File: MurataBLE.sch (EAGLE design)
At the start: 46 parts, among them CON1 C-2235, IC1 I-5448, IC3 74LVC1G00DBV, Q1 FC-135 32.7680KA-AG3, Q2 12MHz, SW1 P8073, SW2 P8073, SW3 P8073, U1 IC_BLE_LBCA2HNZYZ-711, X1 TSW-114-02-S-S

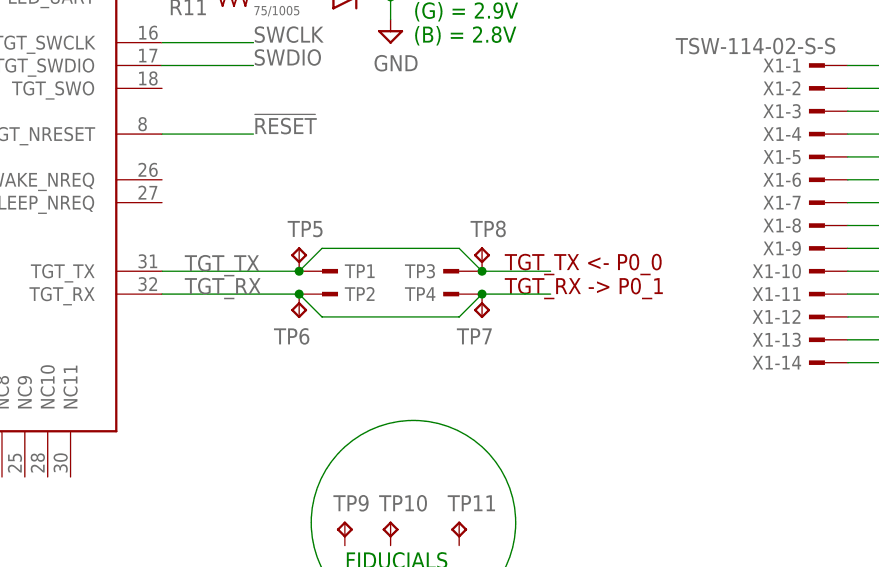
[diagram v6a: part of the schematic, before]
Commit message: [ USB ][ SCH ] test pads are connected
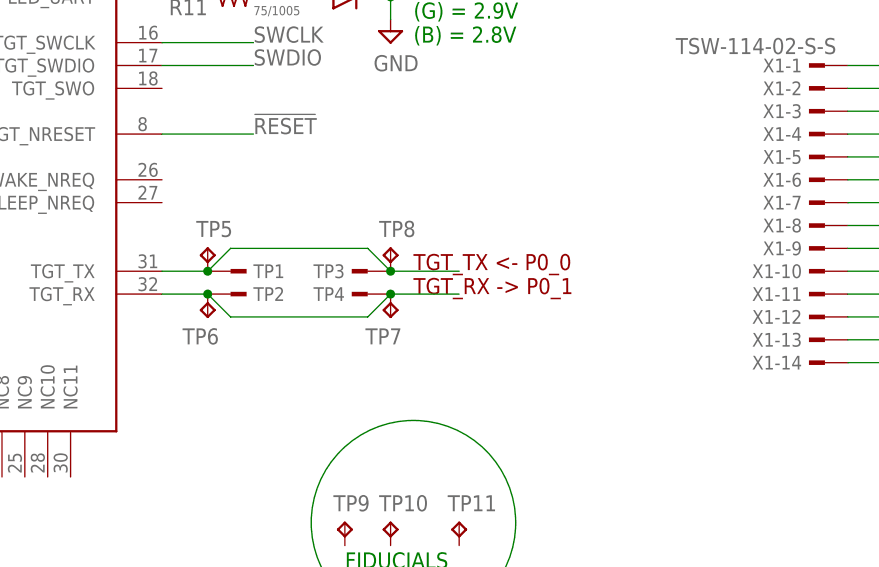
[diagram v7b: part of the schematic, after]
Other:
- moved on the sheet: TP1, TP2, TP3, TP4, TP5, TP6, TP7, TP8
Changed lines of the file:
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@@
 (G) = 2.9V
 (B) = 2.8V</text>
-<text x="195.58" y="68.58" size="1.778" layer="94">TGT_TX &lt;- P0_0
+<text x="185.42" y="68.58" size="1.778" layer="94">TGT_TX &lt;- P0_0
 TGT_RX -&gt; P0_1</text>
 <text x="233.68" y="139.7" size="1.778" layer="94">P0_0 -&gt; TGT_TX
@@
 <instance part="LED1" gate="G" x="175.26" y="104.14" rot="R90"/>
 <instance part="LED1" gate="B" x="177.8" y="101.6" rot="R90"/>
-<instance part="TP5" gate="G$1" x="172.72" y="73.66"/>
-<instance part="TP6" gate="G$1" x="172.72" y="66.04" rot="R180"/>
-<instance part="TP7" gate="G$1" x="193.04" y="66.04" rot="R180"/>
-<instance part="TP8" gate="G$1" x="193.04" y="73.66"/>
+<instance part="TP5" gate="G$1" x="162.56" y="73.66"/>
+<instance part="TP6" gate="G$1" x="162.56" y="66.04" rot="R180"/>
+<instance part="TP7" gate="G$1" x="182.88" y="66.04" rot="R180"/>
+<instance part="TP8" gate="G$1" x="182.88" y="73.66"/>
 <instance part="X1" gate="-1" x="231.14" y="93.98" rot="MR0"/>
 <instance part="X1" gate="-2" x="231.14" y="91.44" rot="MR0"/>
@@
 <instance part="X1" gate="-13" x="231.14" y="63.5" rot="MR0"/>
 <instance part="X1" gate="-14" x="231.14" y="60.96" rot="MR0"/>
-<instance part="TP1" gate="1" x="175.26" y="71.12"/>
-<instance part="TP2" gate="1" x="175.26" y="68.58"/>
-<instance part="TP3" gate="1" x="190.5" y="71.12" rot="R180"/>
-<instance part="TP4" gate="1" x="190.5" y="68.58" rot="R180"/>
+<instance part="TP1" gate="1" x="165.1" y="71.12"/>
+<instance part="TP2" gate="1" x="165.1" y="68.58"/>
+<instance part="TP3" gate="1" x="180.34" y="71.12" rot="R180"/>
+<instance part="TP4" gate="1" x="180.34" y="68.58" rot="R180"/>
 <instance part="TP9" gate="G$1" x="177.8" y="43.18"/>
 <instance part="TP10" gate="G$1" x="182.88" y="43.18"/>
@@
 <segment>
 <pinref part="IC2" gate="G$1" pin="TGT_TX"/>
-<label x="160.02" y="71.12" size="1.778" layer="95"/>
-<wire x1="172.72" y1="71.12" x2="157.48" y2="71.12" width="0.1524" layer="91"/>
+<wire x1="162.56" y1="71.12" x2="157.48" y2="71.12" width="0.1524" layer="91"/>
 <pinref part="TP5" gate="G$1" pin="TP"/>
-<junction x="172.72" y="71.12"/>
+<junction x="162.56" y="71.12"/>
 <pinref part="TP1" gate="1" pin="1"/>
-<wire x1="200.66" y1="71.12" x2="193.04" y2="71.12" width="0.1524" layer="91"/>
+<wire x1="190.5" y1="71.12" x2="182.88" y2="71.12" width="0.1524" layer="91"/>
 <pinref part="TP8" gate="G$1" pin="TP"/>
-<junction x="193.04" y="71.12"/>
+<junction x="182.88" y="71.12"/>
 <pinref part="TP3" gate="1" pin="1"/>
-<wire x1="172.72" y1="71.12" x2="175.26" y2="73.66" width="0.1524" layer="91"/>
-<wire x1="175.26" y1="73.66" x2="190.5" y2="73.66" width="0.1524" layer="91"/>
-<wire x1="190.5" y1="73.66" x2="193.04" y2="71.12" width="0.1524" layer="91"/>
+<wire x1="162.56" y1="71.12" x2="165.1" y2="73.66" width="0.1524" layer="91"/>
+<wire x1="165.1" y1="73.66" x2="180.34" y2="73.66" width="0.1524" layer="91"/>
+<wire x1="180.34" y1="73.66" x2="182.88" y2="71.12" width="0.1524" layer="91"/>
 </segment>
 </net>
@@
 <net name="TGT_RX" class="0">
 <segment>
-<wire x1="200.66" y1="68.58" x2="193.04" y2="68.58" width="0.1524" layer="91"/>
+<wire x1="190.5" y1="68.58" x2="182.88" y2="68.58" width="0.1524" layer="91"/>
 <pinref part="TP7" gate="G$1" pin="TP"/>
-<junction x="193.04" y="68.58"/>
+<junction x="182.88" y="68.58"/>
 <pinref part="TP4" gate="1" pin="1"/>
 <pinref part="IC2" gate="G$1" pin="TGT_RX"/>
-<label x="160.02" y="68.58" size="1.778" layer="95"/>
-<wire x1="172.72" y1="68.58" x2="157.48" y2="68.58" width="0.1524" layer="91"/>
+<wire x1="162.56" y1="68.58" x2="157.48" y2="68.58" width="0.1524" layer="91"/>
 <pinref part="TP6" gate="G$1" pin="TP"/>
-<junction x="172.72" y="68.58"/>
+<junction x="162.56" y="68.58"/>
 <pinref part="TP2" gate="1" pin="1"/>
-<wire x1="193.04" y1="68.58" x2="190.5" y2="66.04" width="0.1524" layer="91"/>
-<wire x1="190.5" y1="66.04" x2="175.26" y2="66.04" width="0.1524" layer="91"/>
-<wire x1="175.26" y1="66.04" x2="172.72" y2="68.58" width="0.1524" layer="91"/>
-</segment>
-</net>
+<wire x1="182.88" y1="68.58" x2="180.34" y2="66.04" width="0.1524" layer="91"/>
+<wire x1="180.34" y1="66.04" x2="165.1" y2="66.04" width="0.1524" layer="91"/>
+<wire x1="165.1" y1="66.04" x2="162.56" y2="68.58" width="0.1524" layer="91"/>
+</segment>
+</net>

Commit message: [ USB ] fix broken schematic link
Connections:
- removed net P0_0: U1.P0_0, X1-5.1
- removed net P0_1: U1.P0_1, X1-4.1
- net TGT_RX: now also U1.P0_1, X1-4.1
- net TGT_TX: now also U1.P0_0, X1-5.1
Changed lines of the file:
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@@
-</segment>
-</net>
-<net name="P0_0" class="0">
-<segment>
-<pinref part="U1" gate="G$1" pin="P0_0"/>
-<wire x1="241.3" y1="142.24" x2="228.6" y2="142.24" width="0.1524" layer="91"/>
-</segment>
-<segment>
-<wire x1="233.68" y1="83.82" x2="241.3" y2="83.82" width="0.1524" layer="91"/>
-<label x="241.3" y="83.82" size="1.778" layer="95"/>
-<pinref part="X1" gate="-5" pin="1"/>
-</segment>
-</net>
-<net name="P0_1" class="0">
-<segment>
-<pinref part="U1" gate="G$1" pin="P0_1"/>
-<wire x1="241.3" y1="139.7" x2="228.6" y2="139.7" width="0.1524" layer="91"/>
-</segment>
-<segment>
-<wire x1="233.68" y1="86.36" x2="241.3" y2="86.36" width="0.1524" layer="91"/>
-<label x="241.3" y="86.36" size="1.778" layer="95"/>
-<pinref part="X1" gate="-4" pin="1"/>
 </segment>
 </net>
@@
 <wire x1="180.34" y1="73.66" x2="182.88" y2="71.12" width="0.1524" layer="91"/>
 </segment>
+<segment>
+<pinref part="U1" gate="G$1" pin="P0_0"/>
+<wire x1="241.3" y1="142.24" x2="228.6" y2="142.24" width="0.1524" layer="91"/>
+</segment>
+<segment>
+<wire x1="233.68" y1="83.82" x2="241.3" y2="83.82" width="0.1524" layer="91"/>
+<label x="241.3" y="83.82" size="1.778" layer="95"/>
+<pinref part="X1" gate="-5" pin="1"/>
+</segment>
 </net>
 <net name="N$4" class="0">
@@
 <wire x1="165.1" y1="66.04" x2="162.56" y2="68.58" width="0.1524" layer="91"/>
 </segment>
-</net>
+<segment>
+<pinref part="U1" gate="G$1" pin="P0_1"/>
+<wire x1="241.3" y1="139.7" x2="228.6" y2="139.7" width="0.1524" layer="91"/>
+</segment>
+<segment>
+<wire x1="233.68" y1="86.36" x2="241.3" y2="86.36" width="0.1524" layer="91"/>
+<label x="241.3" y="86.36" size="1.778" layer="95"/>
+<pinref part="X1" gate="-4" pin="1"/>
+</segment>
+</net>
